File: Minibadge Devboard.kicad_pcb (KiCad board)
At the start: 2 copper layers, 30.5 x 48.3 mm, 45 parts, among them J1 External power, J2 External switch, SW1 Power, SW3 SPEED, SW4 NTC

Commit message: Update values
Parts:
- C11: value C_SS -> 0.1uF
- CHARGE: value RED -> CHARGE
- PWR: value RED -> PWR
- R9: value R_ILIM -> 30kΩ
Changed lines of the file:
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@@
 			)
 		)
-		(property "LCSC Part #" ""
+		(property "LCSC Part #" "C8218"
 			(at 0 0 180)
 			(unlocked yes)
@@
 			)
 		)
-		(property "Value" "C_SS"
+		(property "Value" "0.1uF"
 			(at 0 1.43 0)
 			(layer "F.Fab")
@@
 			)
 		)
-		(property "LCSC Part #" ""
+		(property "LCSC Part #" "C14663"
 			(at 0 0 0)
 			(unlocked yes)
@@
 			)
 		)
-		(property "Value" "R_ILIM"
+		(property "Value" "30kΩ"
 			(at 0 1.43 0)
 			(layer "F.Fab")
@@
 			)
 		)
-		(property "LCSC Part #" ""
+		(property "LCSC Part #" "C22984"
 			(at 0 0 0)
 			(unlocked yes)
@@
 			)
 		)
-		(property "Value" "RED"
+		(property "Value" "CHARGE"
 			(at 0 1.43 0)
 			(layer "F.Fab")
@@
 			)
 		)
-		(property "LCSC Part #" ""
+		(property "LCSC Part #" "C8218"
 			(at 0 0 0)
 			(unlocked yes)
@@
 			)
 		)
-		(property "Value" "RED"
+		(property "Value" "PWR"
 			(at 0 1.43 0)
 			(layer "F.Fab")

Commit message: Update Minibadge Devboard.kicad_pcb
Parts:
- added ?: , , F.Cu at (104.1, 81.3)
- added ?: , , F.Cu at (94.0, 81.3)
- added ?: , , F.Cu at (114.3, 81.3)
- added ?: , , F.Cu at (101.6, 81.3)
- added ?: , , F.Cu at (96.5, 81.3)
- added ?: , , F.Cu at (106.7, 81.3)
- added ?: , , F.Cu at (111.8, 81.3)
- added ?: , , F.Cu at (91.4, 81.3)
- added ?: , , F.Cu at (116.8, 81.3)
- moved JT1 3.85 mm to (114.3, 73.7)
- moved JT2 3.85 mm to (104.1, 73.7)
- moved JT3 3.85 mm to (94.0, 73.7)
- moved NT1 3.46 mm to (111.3, 72.9)
- moved C10 2.09 mm to (110.7, 67.6)
- moved C8 2.09 mm to (101.3, 67.6)
- moved JC1 2.09 mm to (114.3, 83.8)
- moved JC2 2.09 mm to (104.1, 83.8)
- moved C1 2.09 mm to (94.1, 51.1)
- moved C11 2.09 mm to (111.0, 53.7)
- moved C4 2.09 mm to (116.9, 43.7)
- moved C7 2.09 mm to (101.3, 58.2)
- moved C9 2.09 mm to (110.7, 58.2)
- moved CHARGE 2.09 mm to (112.8, 37.1)
- moved CLK1 2.09 mm to (99.0, 49.9)
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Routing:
- net -BATT: track 10.5 -> 0.00 mm, vias 4 -> 0
- net NTC: track 45.4 -> 36.6 mm, vias 7 -> 1
- net SYS: track 66.3 -> 60.5 mm, vias 11 -> 6
- net CLK: track 28.4 -> 30.6 mm, vias 7 -> 1
- net GND: track 16.8 -> 19.0 mm, vias 47 -> 42
- net +3.3V-3: track 21.6 -> 22.6 mm, vias 6 -> 0
- net +3.3V-1: track 45.6 -> 46.0 mm, vias 6 -> 0
- net +BATT: track 54.7 -> 54.5 mm, vias 5 -> 0
- net +3.3V-2: track 19.1 -> 18.9 mm, vias 6 -> 0

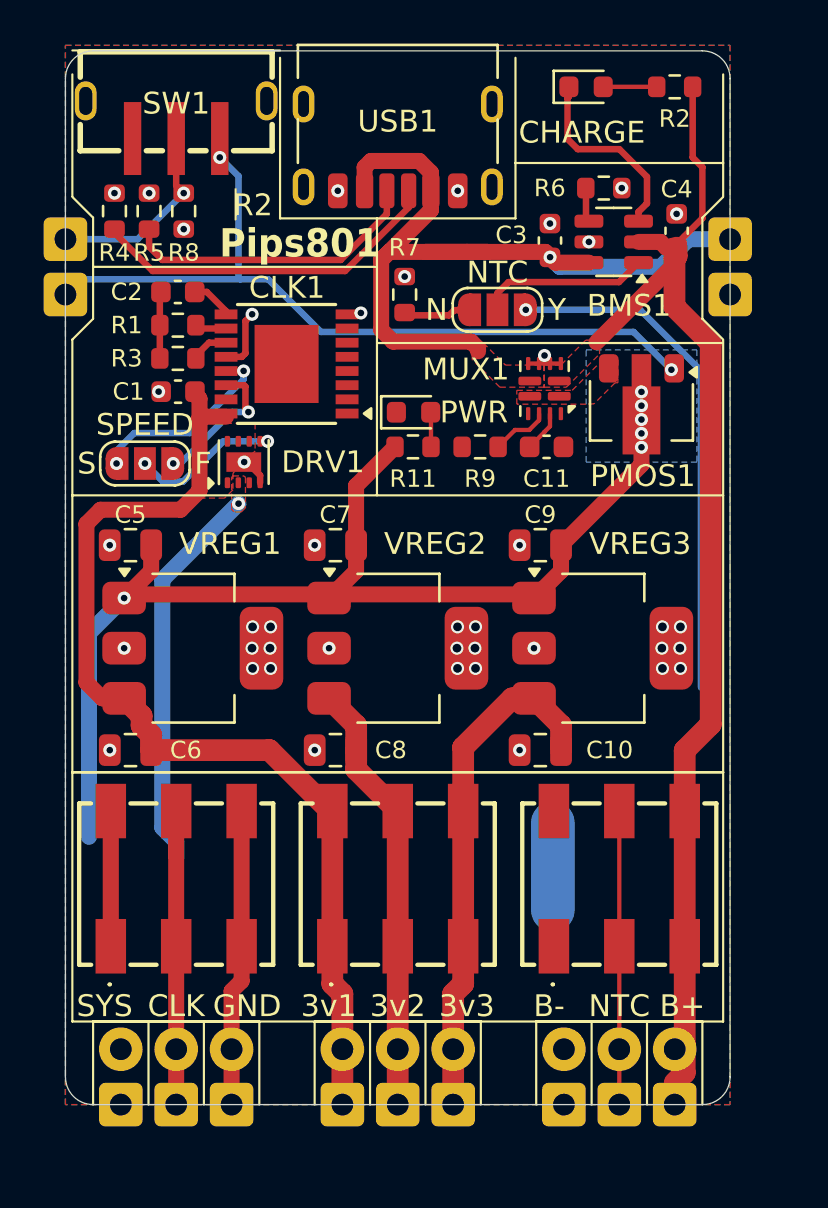
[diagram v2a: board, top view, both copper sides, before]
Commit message: Swap LDO to DC-DC
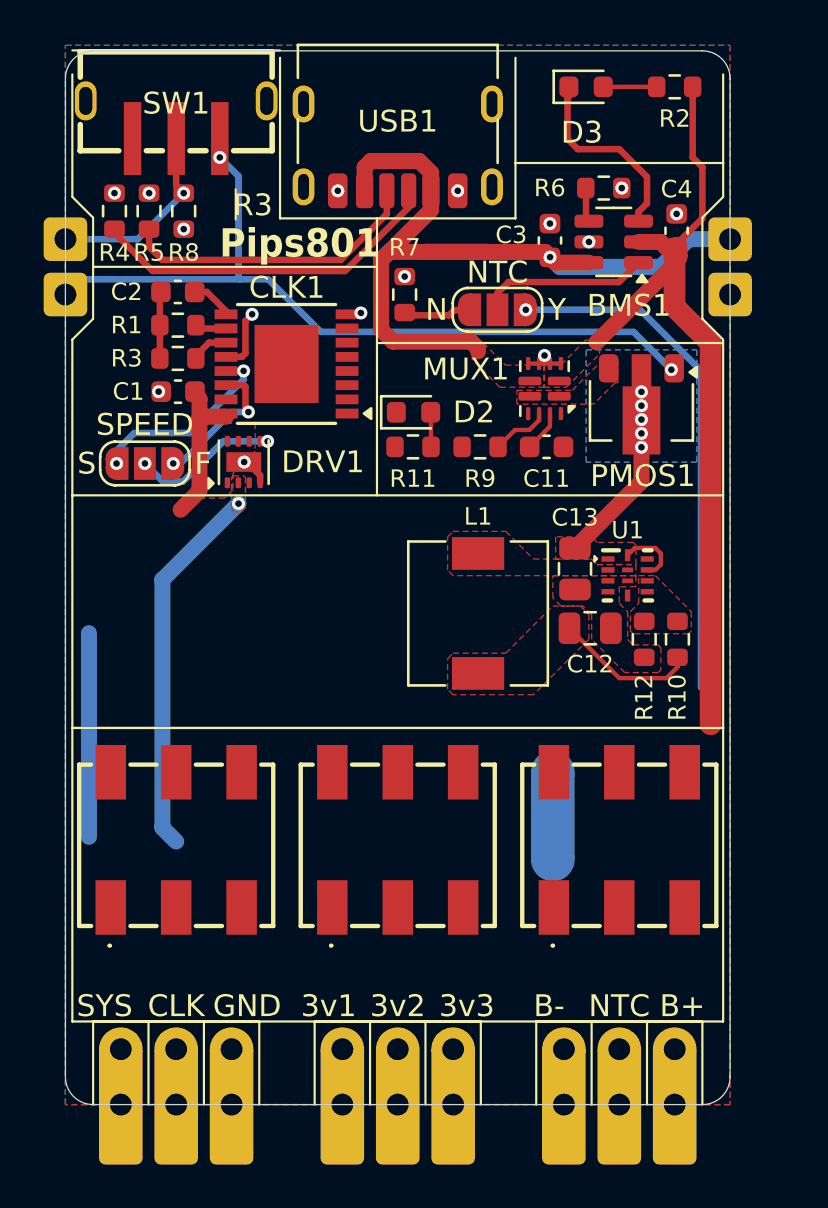
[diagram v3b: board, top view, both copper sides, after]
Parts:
- removed C10, C5, C6, C7, C8, C9: 4.7uF, Capacitor_SMD:C_0805_2012Metric
- removed VREG1, VREG2, VREG3: AP7361C-33E, Package_TO_SOT_SMD:SOT-223-3_TabPin2
- added C12: 10uF, Capacitor_SMD:C_0805_2012Metric, F.Cu at (113.0, 62.0)
- added C13: 10uF, Capacitor_SMD:C_0805_2012Metric, F.Cu at (112.3, 59.2)
- added L1: 1uH, Inductor_SMD:L_6.3x6.3_H3, F.Cu at (107.8, 61.3)
- added R10: 150k, Resistor_SMD:R_0603_1608Metric, F.Cu at (117.0, 62.5)
- added R12: 33k, Resistor_SMD:R_0603_1608Metric, F.Cu at (115.4, 62.5)
- added U1: TI TLV62585RWTR, TI TLV62585RWTR:TLV62585RWTR, F.Cu at (114.7, 59.6)
- moved NT1 2.32 mm to (111.3, 70.6)
- moved JT1 1.78 mm to (114.3, 72.0)
- moved JT2 1.78 mm to (104.1, 72.0)
- moved JT3 1.78 mm to (94.0, 72.0)
- renumbered PWR to D2, CHARGE to D3
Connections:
- SW1 pad 4: GND -> (no net)
- SW1 pad 5: GND -> (no net)
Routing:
- net +3.3V-1: track 46.0 -> 7.10 mm
- net SYS: track 60.5 -> 21.8 mm, vias 6 -> 5
- net +3.3V-3: track 22.6 -> 0.00 mm
- net +3.3V-2: track 18.9 -> 0.00 mm
- net +BATT: track 54.5 -> 37.4 mm
- net CLK: track 30.6 -> 17.2 mm
- net NTC: track 36.6 -> 23.7 mm
- net GND: track 19.0 -> 6.24 mm, vias 42 -> 15
- net +3.3V: track 0.00 -> 6.56 mm
- added copper zone on F.Cu, net +3.3V
- added copper zone on F.Cu, net Net-(L1-Pad1)
- added copper zone on F.Cu, net Net-(U1-FB)
- added copper zone on F.Cu, net SYS

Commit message: Implement/route DC-DC buck
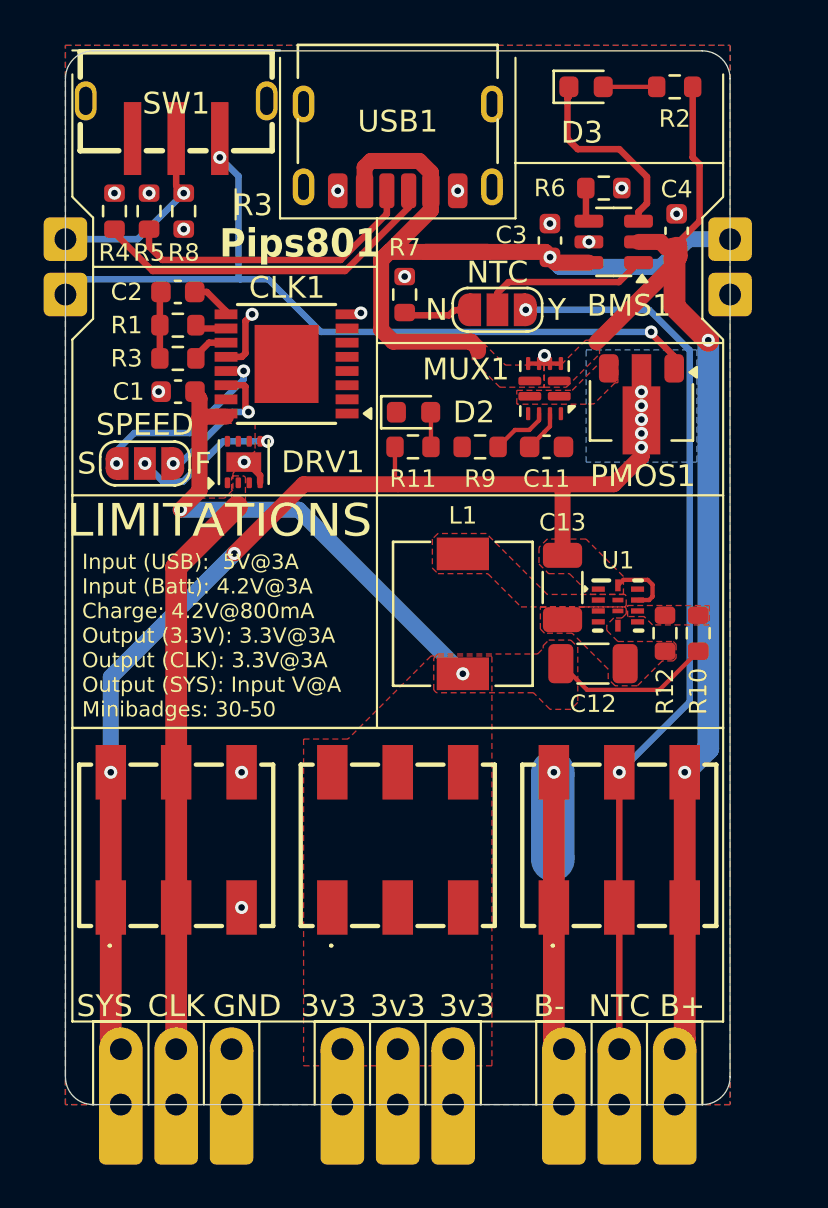
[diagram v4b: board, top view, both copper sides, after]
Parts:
- C12: value 10uF -> 45uF; footprint Capacitor_SMD:C_0805_2012Metric -> Capacitor_SMD:C_1206_3216Metric
- C13: footprint Capacitor_SMD:C_0805_2012Metric -> Capacitor_SMD:C_1206_3216Metric
- moved C12 1.63 mm to (113.1, 63.6)
- moved U1 1.45 mm to (114.2, 60.9)
- moved C13 1.03 mm to (111.7, 60.1)
- moved R10 0.99 mm to (117.9, 62.2)
- moved R12 0.99 mm to (116.4, 62.2)
- moved L1 0.70 mm to (107.1, 61.3)
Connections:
- ? pad 2: +3.3V-2 -> +3.3V
- ? pad 1: +3.3V-1 -> +3.3V
- ? pad 3: +3.3V-3 -> +3.3V
- C1 pad 1: +3.3V-1 -> +3.3V
- CLK1 pad 16: +3.3V-1 -> +3.3V
- DRV1 pad 1: +3.3V-1 -> +3.3V
- DRV1 pad 6: +3.3V-1 -> +3.3V
- DRV1 pad 7: +3.3V-1 -> +3.3V
- DRV1 pad 8: +3.3V-1 -> +3.3V
- JC2 pad 1: +3.3V-1 -> +3.3V
- JC2 pad 2: +3.3V-2 -> +3.3V
- JC2 pad 3: +3.3V-3 -> +3.3V
- JT2 pad 1: +3.3V-1 -> +3.3V
- JT2 pad 2: +3.3V-2 -> +3.3V
- JT2 pad 3: +3.3V-3 -> +3.3V
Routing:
- net SYS: track 21.8 -> 57.9 mm, vias 5 -> 7
- net +3.3V: track 6.56 -> 30.7 mm, vias 0 -> 2
- net NTC: track 23.7 -> 41.7 mm, vias 1 -> 2
- net +BATT: track 37.4 -> 52.8 mm, vias 0 -> 2
- net -BATT: track 0.00 -> 12.9 mm, vias 0 -> 1
- net CLK: track 17.2 -> 26.0 mm, vias 1 -> 0
- net +3.3V-1: track 7.10 -> 0.00 mm
- net GND: vias 15 -> 17
- removed copper zone on F.Cu, net +3.3V-1
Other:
- board text added: "Input (USB): 5V@3A Input (Batt): 4.2V@3A Charge: 4.2V@800mA Output (3.3V): 3.3V@3A Output (CLK): 3.3V@3A Output (SYS): Input V@A Minibadges: 30-50"
- board text added: "LIMITATIONS"
- board text removed: "3v1"
- board text removed: "3v2"

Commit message: Update inductor
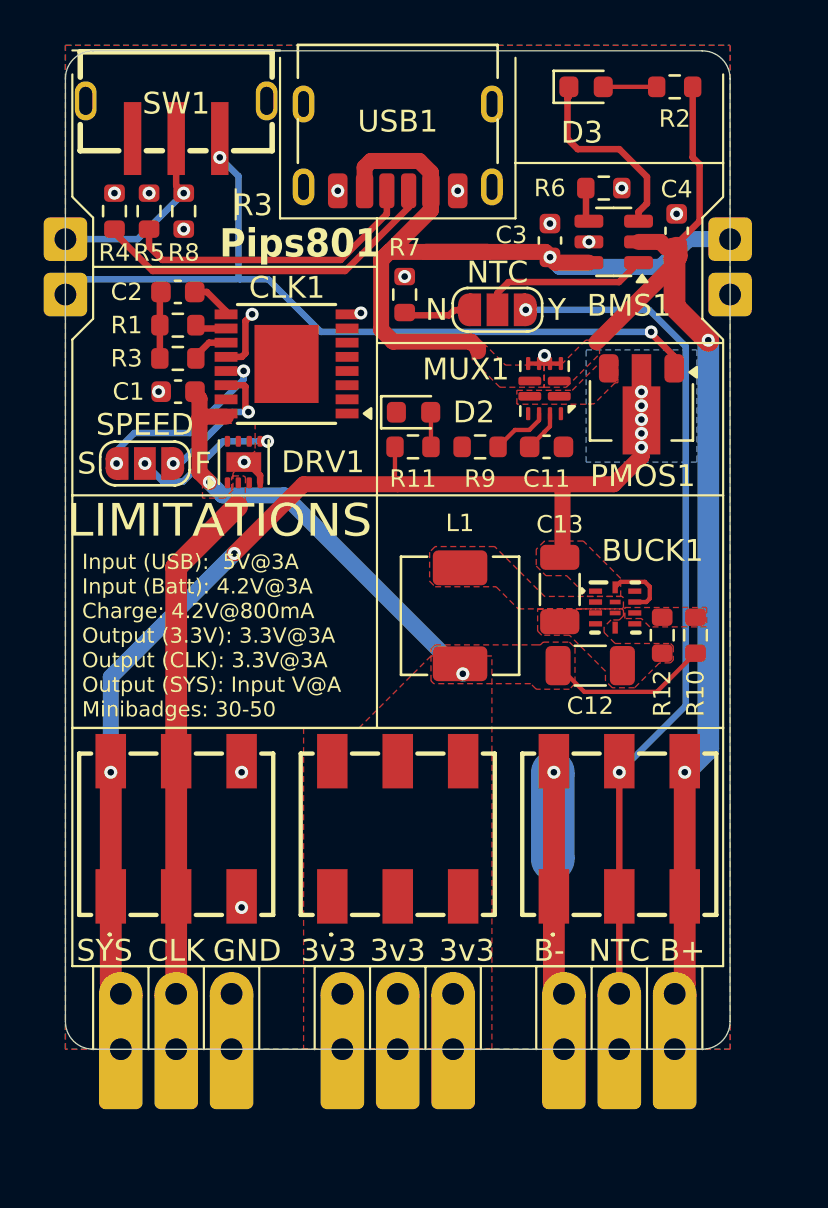
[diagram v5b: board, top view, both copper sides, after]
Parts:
- C12: value 45uF -> 47uF
- C13: value 10uF -> 47uF
- L1: footprint Inductor_SMD:L_6.3x6.3_H3 -> Inductor_SMD:L_KOHERelec_MDA5030
- moved ? 2.54 mm to (104.1, 78.7)
- moved ? 2.54 mm to (94.0, 78.7)
- moved ? 2.54 mm to (114.3, 78.7)
- moved ? 2.54 mm to (101.6, 78.7)
- moved ? 2.54 mm to (96.5, 78.7)
- moved ? 2.54 mm to (106.7, 78.7)
- moved ? 2.54 mm to (111.8, 78.7)
- moved ? 2.54 mm to (91.4, 78.7)
- moved ? 2.54 mm to (116.8, 78.7)
- moved JC1 2.54 mm to (114.3, 81.3)
- moved JC2 2.54 mm to (104.1, 81.3)
- moved JC3 2.54 mm to (94.0, 81.3)
- moved JT1 0.51 mm to (114.3, 71.4)
- moved JT2 0.51 mm to (104.1, 71.4)
- moved JT3 0.51 mm to (94.0, 71.4)
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- renumbered U1 to BUCK1
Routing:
- net +3.3V: track 30.7 -> 28.5 mm
- net NTC: track 41.7 -> 39.5 mm
- net SYS: track 57.9 -> 55.9 mm
- net CLK: track 26.0 -> 24.0 mm
- net -BATT: track 12.9 -> 10.9 mm
- net +BATT: track 52.8 -> 50.8 mm
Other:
- board size 30.5 x 48.3 mm -> 30.5 x 45.8 mm

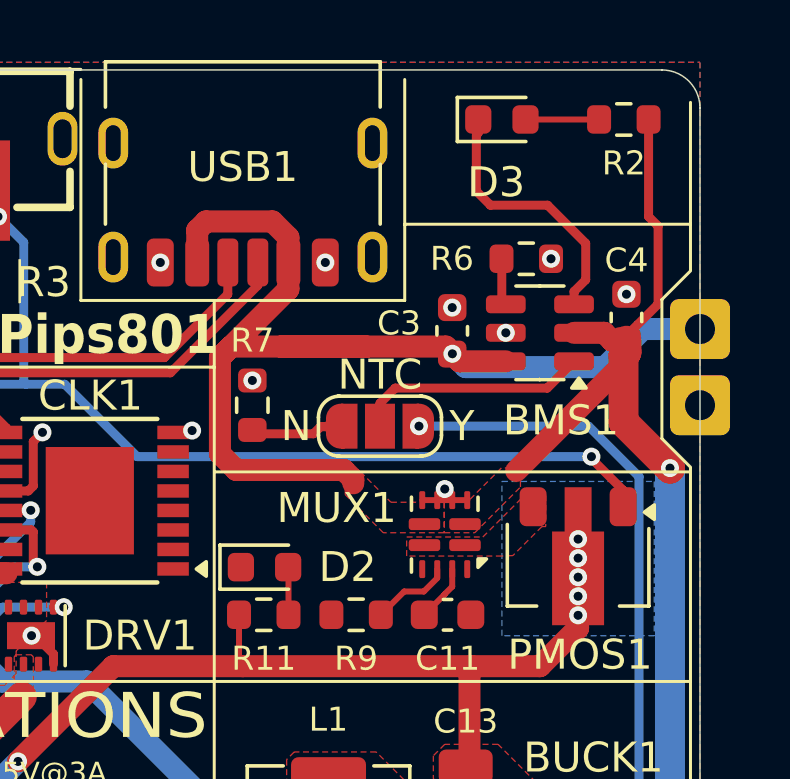
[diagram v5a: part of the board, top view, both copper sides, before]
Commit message: Fix Silkscreen indicators
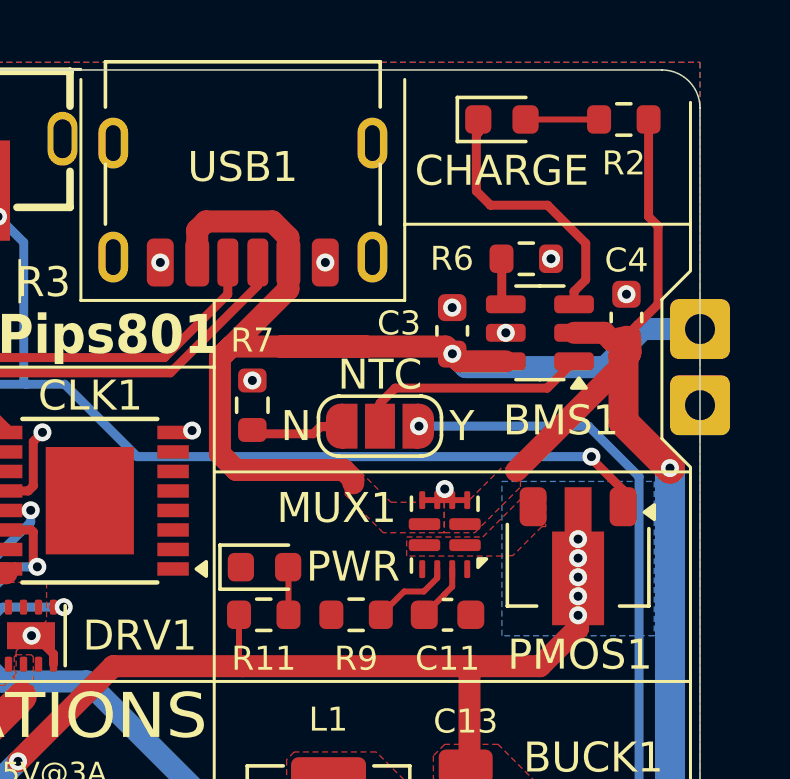
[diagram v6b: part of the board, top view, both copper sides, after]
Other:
- board text added: "CHARGE"
- board text added: "PWR"
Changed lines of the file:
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@@
 			(at -0.1905 2.0955 0)
 			(layer "F.SilkS")
+			(hide yes)
 			(effects
 				(font
@@
 			(at 2.7685 0 0)
 			(layer "F.SilkS")
+			(hide yes)
 			(effects
 				(font
@@
 		)
 	)
+	(gr_text "CHARGE"
+		(at 112.776 38.862 0)
+		(layer "F.SilkS")
+		(effects
+			(font
+				(size 1 1)
+				(thickness 0.15)
+			)
+		)
+	)
 	(gr_text "B-"
 		(at 110.363 77.343 0)
@@
 		)
 	)
+	(gr_text "PWR"
+		(at 107.816487 52.056446 0)
+		(layer "F.SilkS")
+		(effects
+			(font
+				(size 1 1)
+				(thickness 0.15)
+			)
+		)
+	)
